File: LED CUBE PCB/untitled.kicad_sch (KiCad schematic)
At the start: 29 parts, among them J1 Conn_01x04, J2 Conn_01x20, J3 Conn_01x20, SW1 RESET, Y1 8MHz, Y2 32.786KHz

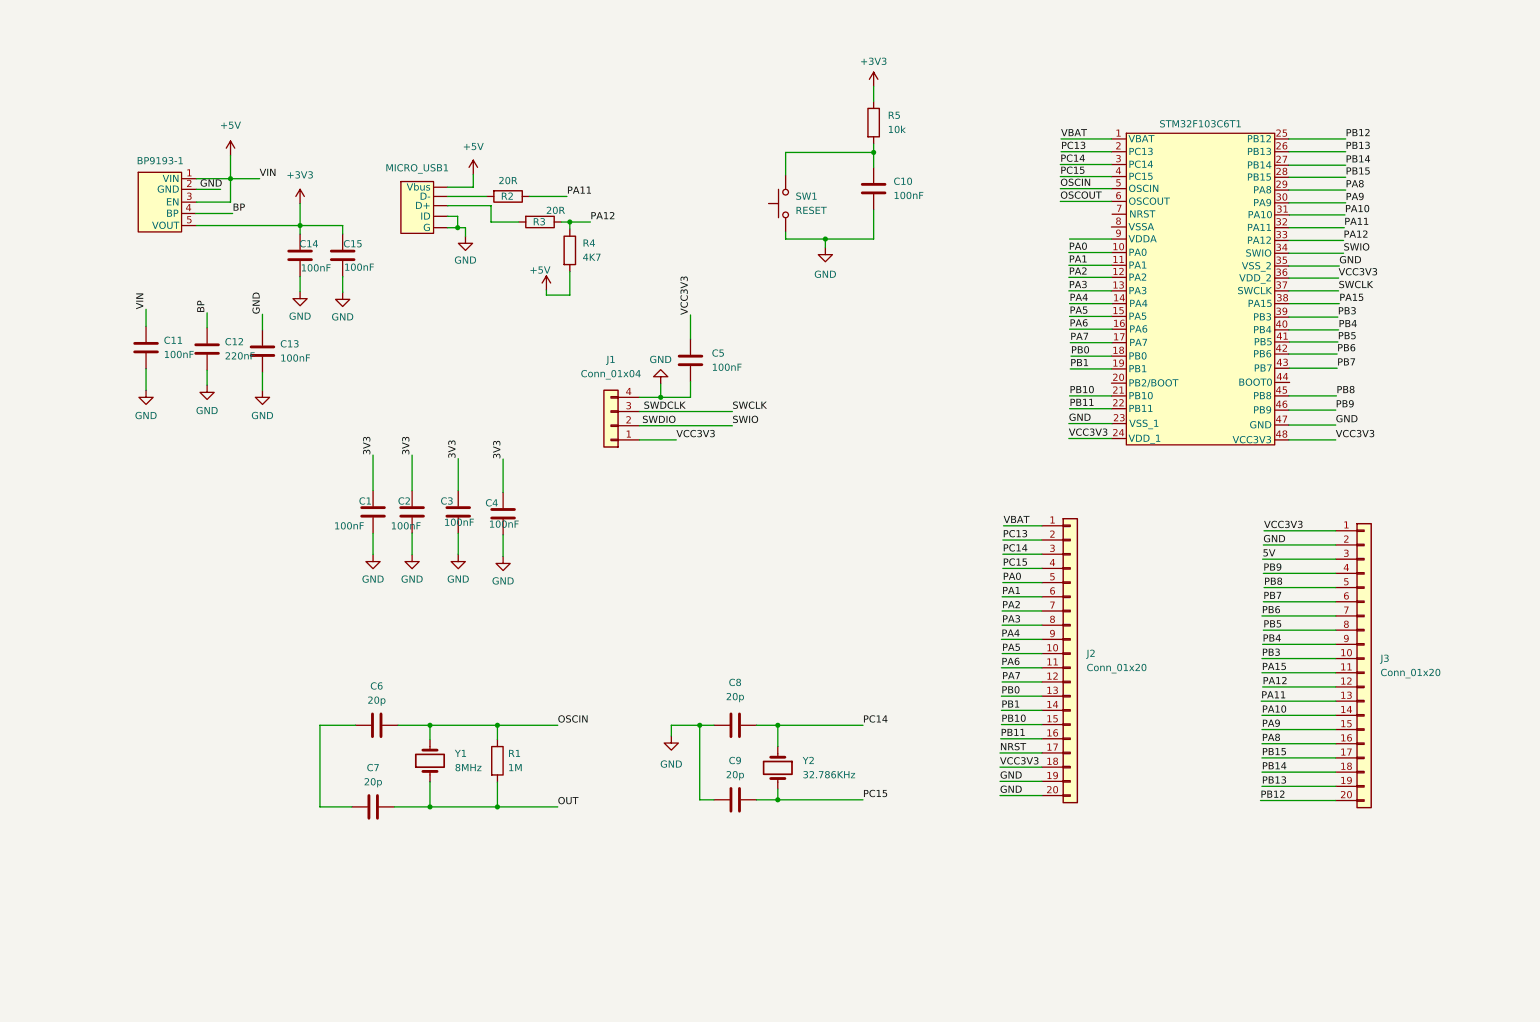
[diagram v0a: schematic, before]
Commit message: Added logic level converter
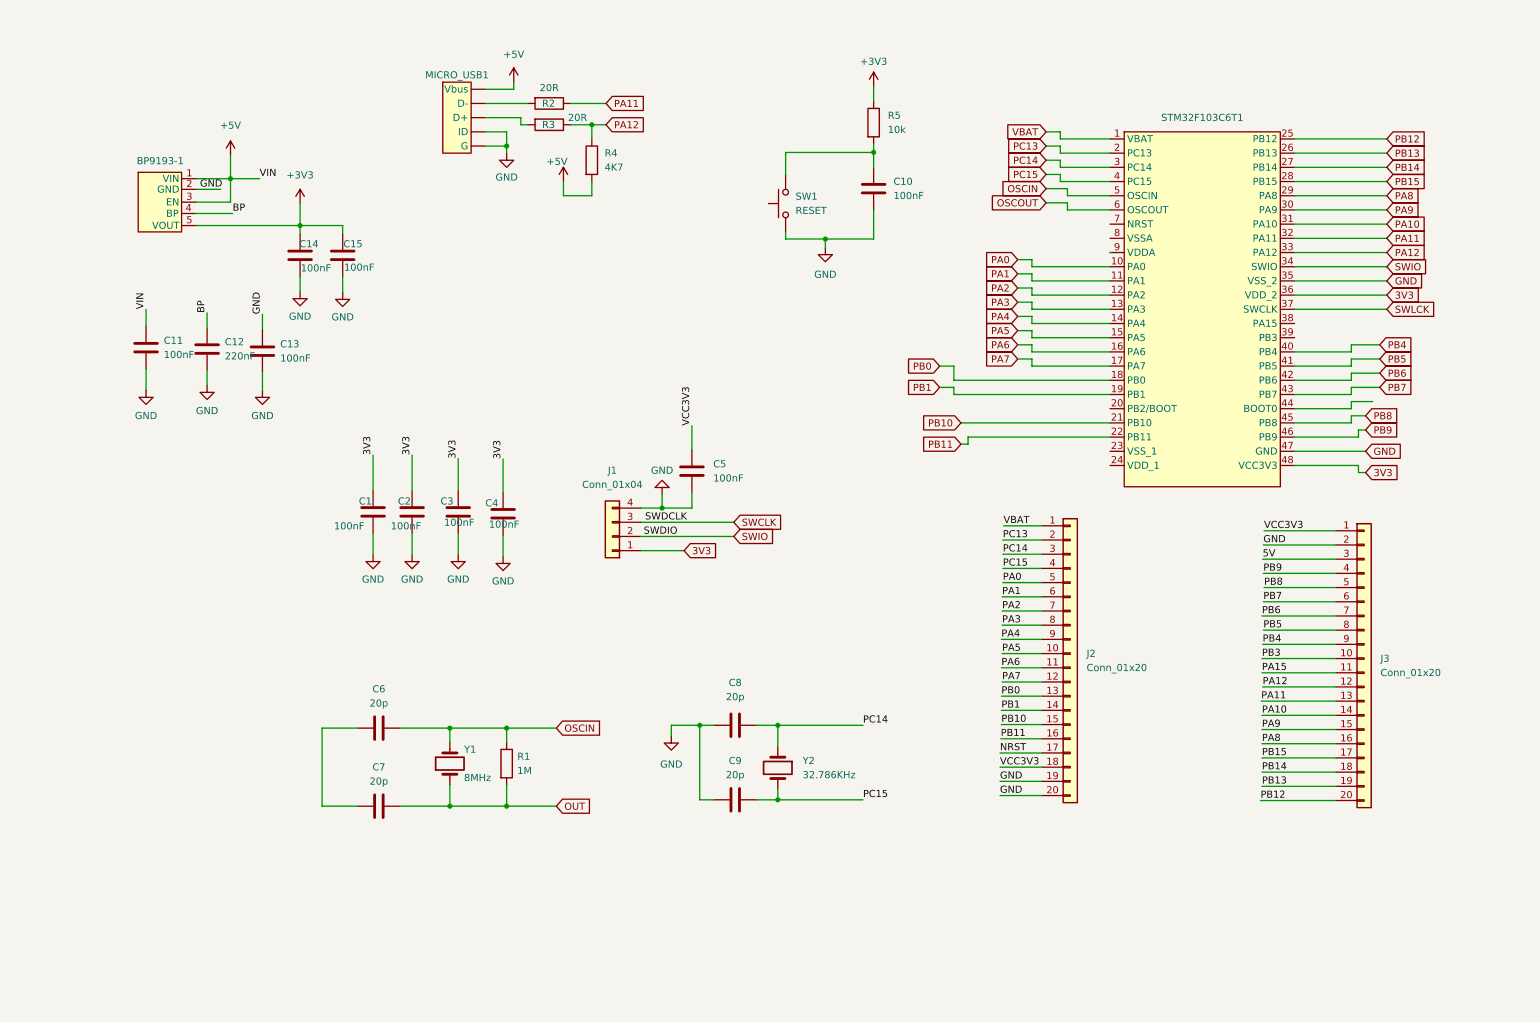
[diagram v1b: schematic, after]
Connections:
- net 3V3: now also STM32F103C6T1.36 (VDD_2), STM32F103C6T1.48 (VCC3V3)
- net GND: no longer STM32F103C6T1.23 (VSS_1)
- net PA15: no longer STM32F103C6T1.38 (PA15)
- net PB3: no longer STM32F103C6T1.39 (PB3)
- net SWCLK: no longer STM32F103C6T1.37 (SWCLK)
- net VCC3V3: no longer J1.1 (Pin_1), STM32F103C6T1.24 (VDD_1), STM32F103C6T1.36 (VDD_2), STM32F103C6T1.48 (VCC3V3)
- net SWDIO renamed SWIO
- new net SWLCK: STM32F103C6T1.37 (SWCLK)
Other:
- moved on the sheet: C5, C6, C7, J1, MICRO_USB1, R1, R2, R3, R4, Y1

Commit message: Push changes
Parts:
- removed J2, J3: Conn_01x20, symbol Connector_Generic:Conn_01x20
- added J1: Conn_01x10, symbol Connector_Generic:Conn_01x10
- STM32F103C6T1: footprint (none) -> STM32F103C8T6_LQFP48:STM32F103C8T6_LQFP
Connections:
- net +3V3: no longer BP9193-1.5 (VOUT), C14.1, C15.1
- net 3V3: now also BP9193-1.5 (VOUT), C14.1, C15.1, J1.1 (Pin_1)
- net 5V: now also J1.5 (Pin_5)
- net GND: now also STM32F103C6T1.23 (VSS_1), STM32F103C6T1.8 (VSSA), J1.6 (Pin_6)
- net PA15: now also STM32F103C6T1.38 (PA15)
- net PB3: now also STM32F103C6T1.39 (PB3)
- net VCC3V3: now also STM32F103C6T1.24 (VDD_1), STM32F103C6T1.9 (VDDA)
- net RESET: now reaches C10.1, R5.2, SW1.2
- net RESET: now also STM32F103C6T1.7 (NRST)
- net BOOT1: now reaches STM32F103C6T1.20 (PB2/BOOT)
- net BOOT0: now reaches STM32F103C6T1.44 (BOOT0)
- new net DIN1: J1.1 (Pin_1)
- new net DIN2: J1.2 (Pin_2)
- new net DIN3: J1.3 (Pin_3)
- new net DIN4: J1.4 (Pin_4)
- new net DIN5: J1.7 (Pin_7)
- new net DIN6: J1.8 (Pin_8)
- new net DIN7: J1.9 (Pin_9)
- new net DIN8: J1.10 (Pin_10)
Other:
- moved on the sheet: BP9193-1, C1, C10, C11, C12, C13, C14, C15, C2, C3, C4, C5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

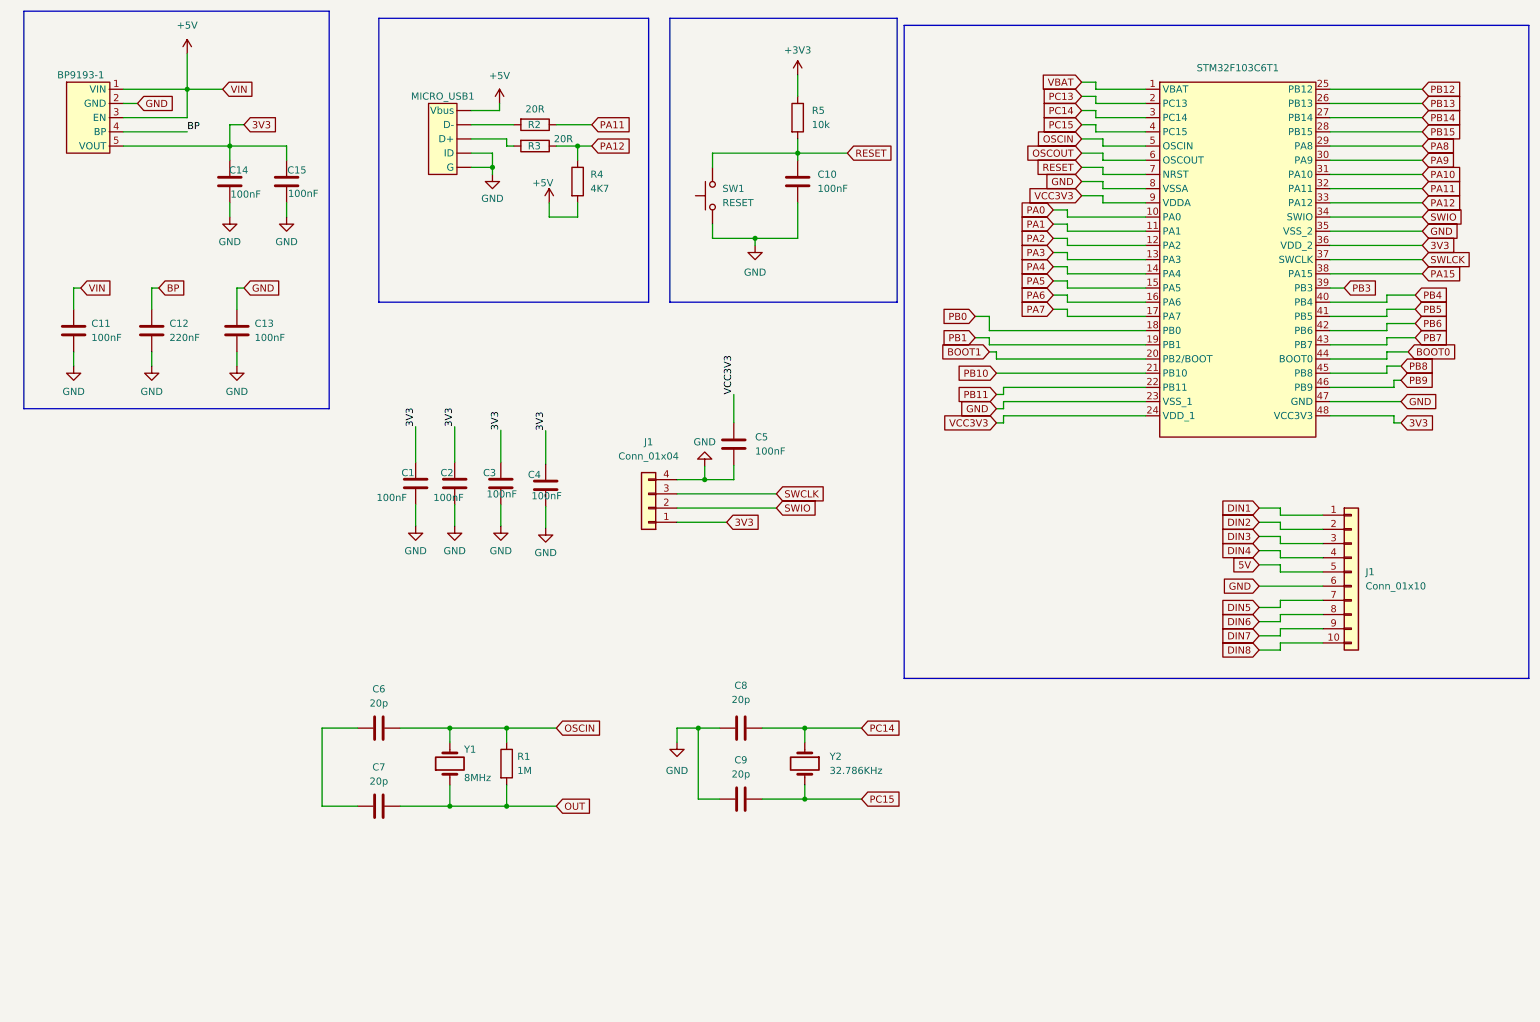
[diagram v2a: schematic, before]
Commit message: Fixed problems on schematic
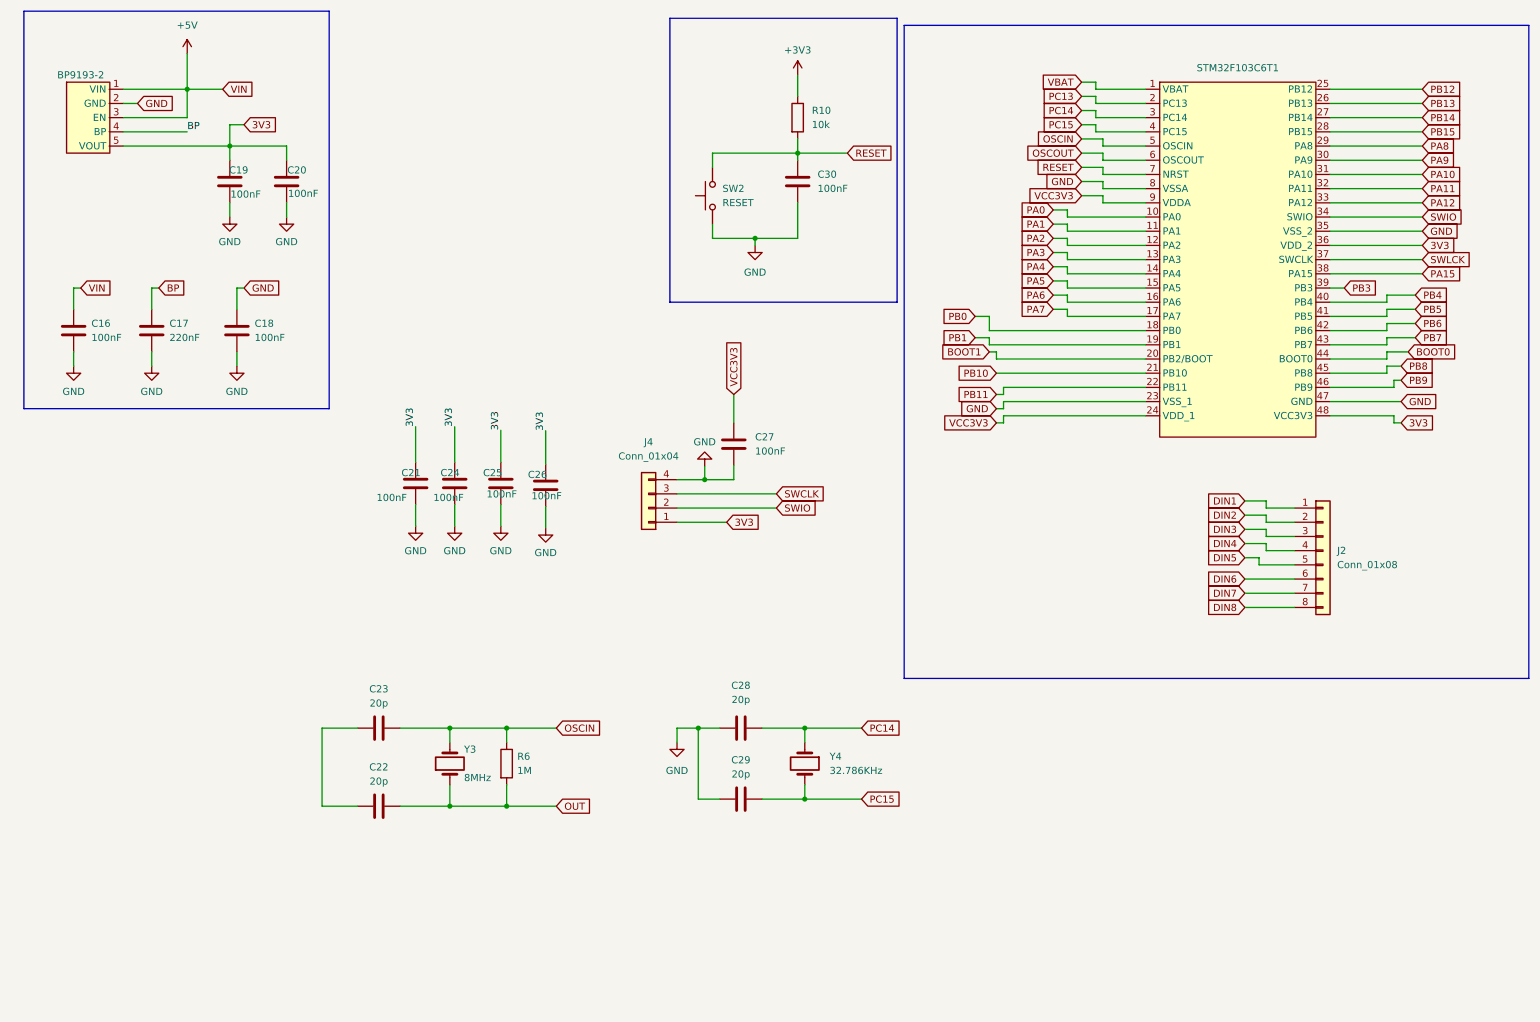
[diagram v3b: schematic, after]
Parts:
- removed J1: Conn_01x10, symbol Connector_Generic:Conn_01x10
- removed MICRO_USB1: ~, symbol USB_MICRO_SYMBOL:MICRO_USB
- removed R2, R3: 20R, Resistor_SMD:R_0201_0603Metric, symbol Device:R
- removed R4: 4K7, Resistor_SMD:R_0201_0603Metric, symbol Device:R
- added J2: Conn_01x08, Connector_PinHeader_2.54mm:PinHeader_1x08_P2.54mm_Vertical, symbol Connector_Generic:Conn_01x08
- C16: renamed from C11; footprint (none) -> Borna KiCAD Library:C0603
- C17: renamed from C12; footprint (none) -> Borna KiCAD Library:C0603
- C18: renamed from C13; footprint (none) -> Borna KiCAD Library:C0603
- J4: renamed from J1; footprint (none) -> Connector_PinHeader_2.54mm:PinHeader_1x04_P2.54mm_Vertical
- STM32F103C6T1: footprint STM32F103C8T6_LQFP48:STM32F103C8T6_LQFP -> Borna KiCAD Library:TQFP48
- renumbered BP9193-1 to BP9193-2, C14 to C19, C15 to C20, C1 to C21, C7 to C22, C6 to C23, C2 to C24, C3 to C25, C4 to C26, C5 to C27, C8 to C28, C9 to C29, C10 to C30, R5 to R10, R1 to R6, SW1 to SW2, Y1 to Y3, Y2 to Y4
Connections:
- net DIN1: now also J2.1 (Pin_1)
- net DIN2: now also J2.2 (Pin_2)
- net DIN3: now also J2.3 (Pin_3)
- net DIN4: now also J2.4 (Pin_4)
- net DIN5: now also J2.5 (Pin_5)
- net DIN6: now also J2.6 (Pin_6)
- net DIN7: now also J2.7 (Pin_7)
- net DIN8: now also J2.8 (Pin_8)

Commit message: Update schema
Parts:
- SW2: footprint (none) -> SMD_PUSH_BUTTON:SMD_BUTTON
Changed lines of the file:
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@@
 			)
 		)
-		(property "Footprint" ""
+		(property "Footprint" "SMD_PUSH_BUTTON:SMD_BUTTON"
 			(at 132.08 45.72 0)
 			(effects

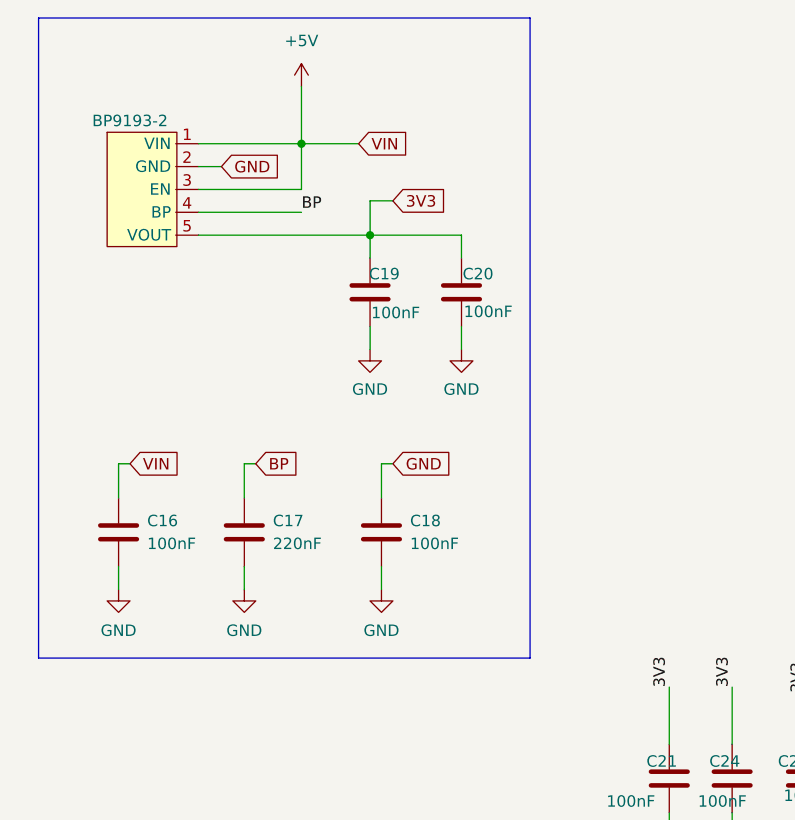
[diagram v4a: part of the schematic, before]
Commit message: Change voltage regulator
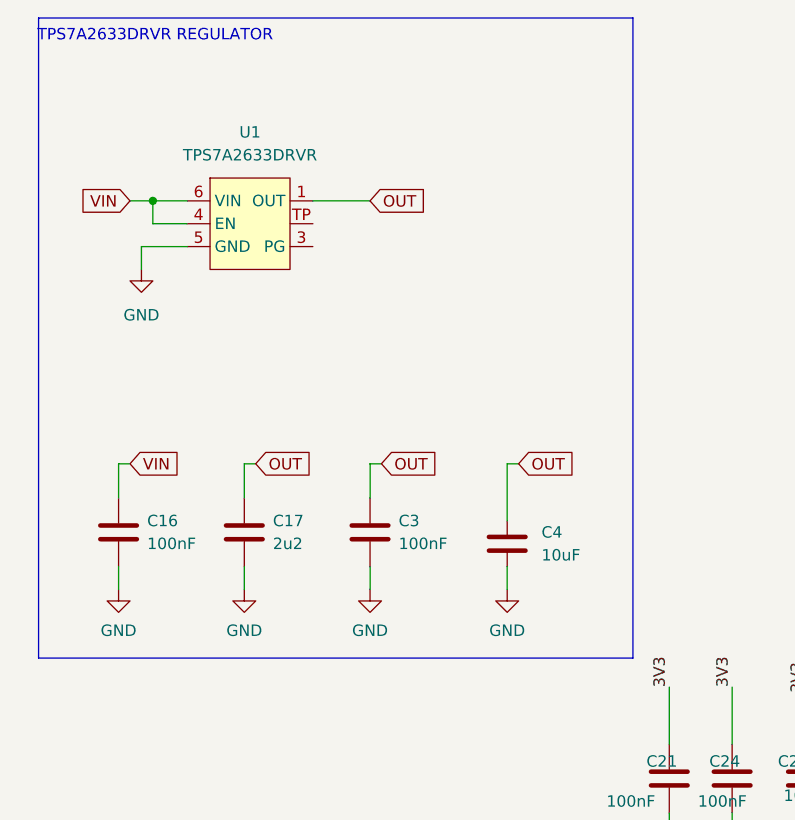
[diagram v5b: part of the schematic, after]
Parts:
- removed BP9193-2: ~, symbol RT9193-33_symbol:RT9193-33
- removed C18: 100nF, Borna KiCAD Library:C0603, symbol Device:C
- removed C19: 100nF, Capacitor_SMD:C_0805_2012Metric, symbol Device:C
- removed C20: 100nF, Capacitor_SMD:C_0603_1608Metric, symbol Device:C
- added C3: 100nF, Borna KiCAD Library:C0603, symbol Device:C
- added C4: 10uF, Borna KiCAD Library:C1206, symbol BornaKiCad:C1206
- added U1: TPS7A2633DRVR, Borna KiCAD Library:WSON-6, symbol BornaKiCad:TPS7A2633DRVR
- C17: value 220nF -> 2u2
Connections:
- net BP is gone; now on net OUT: C17.1
- net GND: now also C3.2, C4.1, U1.5 (GND)
- net OUT: now also C3.1, C4.2, U1.1 (OUT)
- net +5V renamed VIN
- net VIN: now also U1.4 (EN), U1.6 (VIN)
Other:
- note added: "TPS7A2633DRVR REGULATOR"
